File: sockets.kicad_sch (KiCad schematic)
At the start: 8 parts

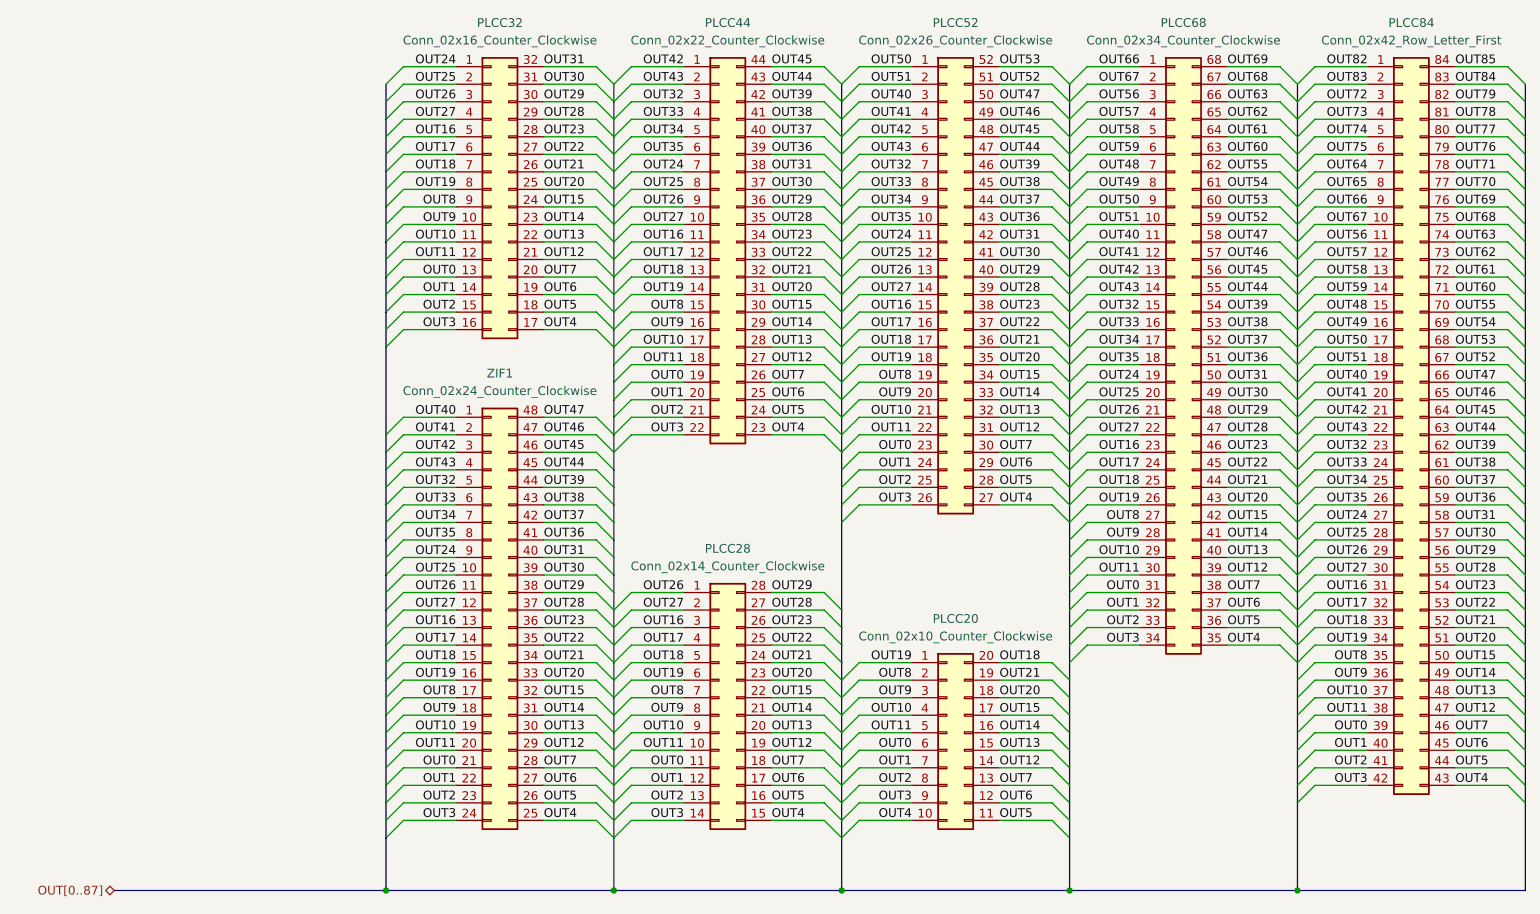
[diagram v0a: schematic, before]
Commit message: updates:
- update symbols and footprints from library
- re-correct 84 pin PLCC pin numbers
- reset transistors to TO-2whatever from SMD
- adjust position of DIN connectors, LEDs and their resistors (and 48 pin DIP and transistors and decoupling capacitors):  measured again.
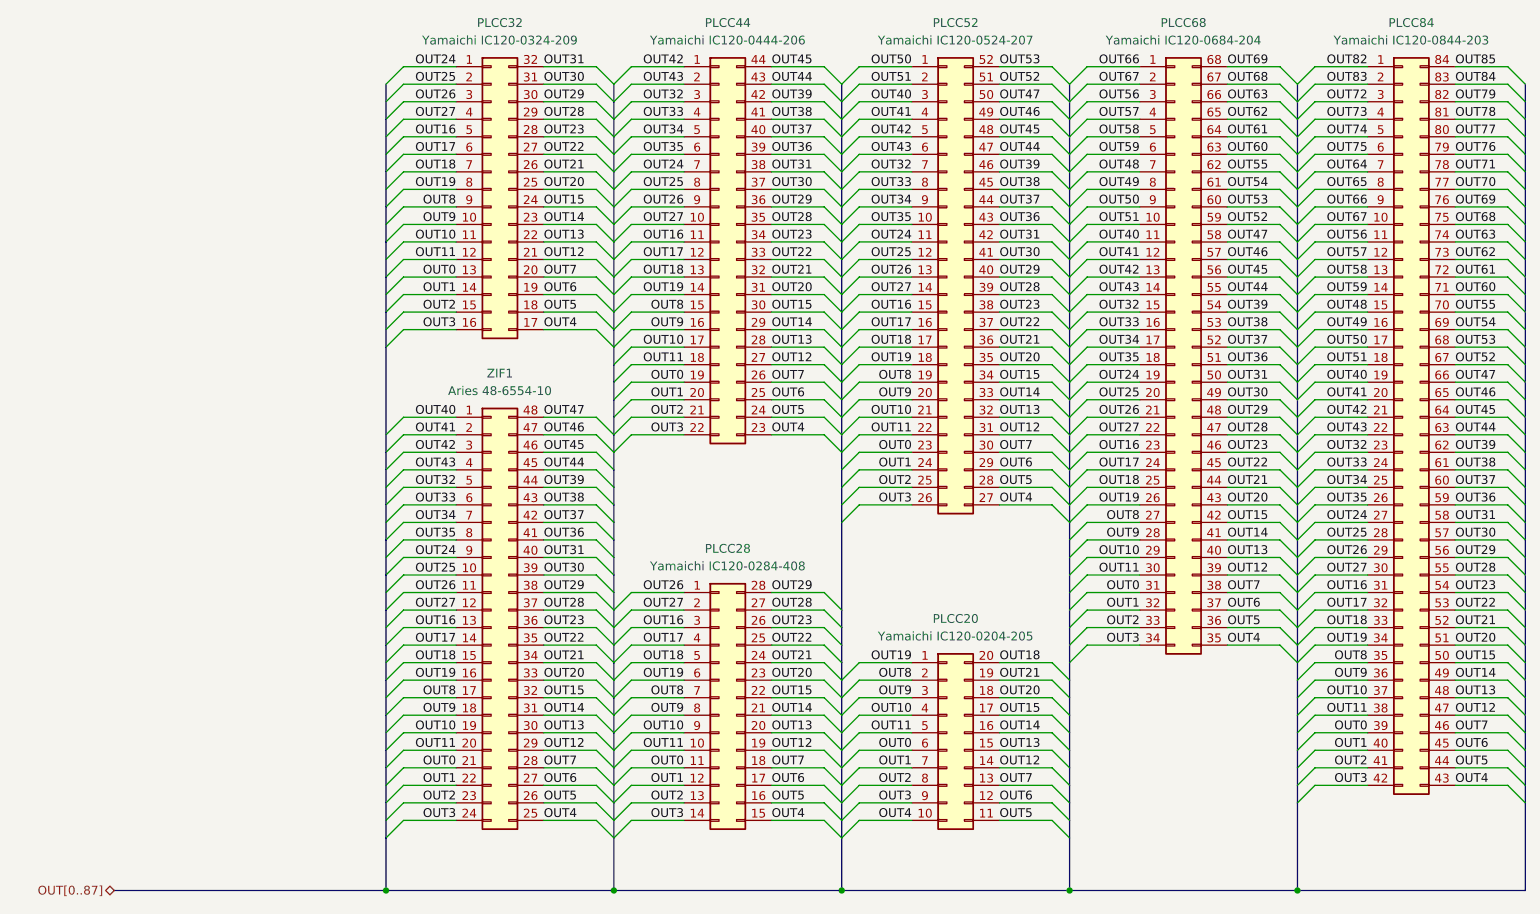
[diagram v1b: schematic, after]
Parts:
- PLCC20: value Conn_02x10_Counter_Clockwise -> Yamaichi IC120-0204-205
- PLCC28: value Conn_02x14_Counter_Clockwise -> Yamaichi IC120-0284-408
- PLCC32: value Conn_02x16_Counter_Clockwise -> Yamaichi IC120-0324-209
- PLCC44: value Conn_02x22_Counter_Clockwise -> Yamaichi IC120-0444-206
- PLCC52: value Conn_02x26_Counter_Clockwise -> Yamaichi IC120-0524-207
- PLCC68: value Conn_02x34_Counter_Clockwise -> Yamaichi IC120-0684-204
- PLCC84: value Conn_02x42_Row_Letter_First -> Yamaichi IC120-0844-203
- ZIF1: value Conn_02x24_Counter_Clockwise -> Aries 48-6554-10
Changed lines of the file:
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@@
 			)
 		)
-		(property "Value" "Conn_02x42_Row_Letter_First"
+		(property "Value" "Yamaichi IC120-0844-203"
 			(at 219.71 34.29 0)
 			(effects
@@
 			)
 		)
+		(pin "8"
+		)
+		(pin "26"
+		)
+		(pin "6"
+		)
+		(pin "30"
+		)
+		(pin "34"
+		)
+		(pin "14"
+		)
+		(pin "29"
+		)
+		(pin "15"
+		)
+		(pin "27"
+		)
+		(pin "12"
+		)
+		(pin "28"
+		)
+		(pin "23"
+		)
+		(pin "11"
+		)
+		(pin "10"
+		)
+		(pin "31"
+		)
+		(pin "32"
+		)
+		(pin "24"
+		)
+		(pin "7"
+		)
+		(pin "33"
+		)
+		(pin "25"
+		)
+		(pin "9"
+		)
+		(pin "13"
+		)
+		(pin "38"
+		)
+		(pin "39"
+		)
+		(pin "78"
+		)
+		(pin "77"
+		)
+		(pin "76"
+		)
+		(pin "81"
+		)
+		(pin "80"
+		)
+		(pin "79"
+		)
+		(pin "75"
+		)
+		(pin "1"
+		)
+		(pin "2"
+		)
+		(pin "84"
+		)
+		(pin "83"
+		)
+		(pin "82"
+		)
+		(pin "74"
+		)
+		(pin "73"
+		)
+		(pin "72"
+		)
+		(pin "71"
+		)
+		(pin "70"
+		)
+		(pin "69"
+		)
+		(pin "65"
+		)
+		(pin "64"
+		)
+		(pin "63"
+		)
+		(pin "35"
+		)
+		(pin "36"
+		)
+		(pin "16"
+		)
+		(pin "62"
+		)
+		(pin "61"
+		)
+		(pin "60"
+		)
+		(pin "68"
+		)
+		(pin "67"
+		)
+		(pin "66"
+		)
+		(pin "54"
+		)
+		(pin "53"
+		)
+		(pin "52"
+		)
+		(pin "47"
+		)
+		(pin "46"
+		)
+		(pin "45"
+		)
+		(pin "57"
+		)
+		(pin "56"
+		)
+		(pin "55"
+		)
+		(pin "17"
+		)
+		(pin "18"
+		)
+		(pin "19"
+		)
+		(pin "44"
+		)
+		(pin "43"
+		)
 		(pin "37"
 		)
-		(pin "8"
-		)
-		(pin "12"
-		)
-		(pin "80"
-		)
-		(pin "14"
-		)
-		(pin "31"
-		)
-		(pin "78"
-		)
-		(pin "84"
-		)
-		(pin "15"
+		(pin "20"
+		)
+		(pin "21"
+		)
+		(pin "22"
+		)
+		(pin "51"
+		)
+		(pin "50"
 		)
 		(pin "49"
 		)
-		(pin "28"
-		)
-		(pin "17"
-		)
-		(pin "44"
-		)
-		(pin "54"
-		)
-		(pin "9"
-		)
-		(pin "19"
-		)
-		(pin "32"
-		)
-		(pin "25"
+		(pin "40"
+		)
+		(pin "41"
+		)
+		(pin "42"
+		)
+		(pin "3"
+		)
+		(pin "4"
+		)
+		(pin "5"
+		)
+		(pin "59"
+		)
+		(pin "58"
 		)
 		(pin "48"
-		)
-		(pin "47"
-		)
-		(pin "45"
-		)
-		(pin "27"
-		)
-		(pin "24"
-		)
-		(pin "72"
-		)
-		(pin "10"
-		)
-		(pin "55"
-		)
-		(pin "57"
-		)
-		(pin "56"
-		)
-		(pin "20"
-		)
-		(pin "21"
-		)
-		(pin "46"
-		)
-		(pin "26"
-		)
-		(pin "39"
-		)
-		(pin "40"
-		)
-		(pin "67"
-		)
-		(pin "66"
-		)
-		(pin "59"
-		)
-		(pin "36"
-		)
-		(pin "41"
-		)
-		(pin "42"
-		)
-		(pin "75"
-		)
-		(pin "74"
-		)
-		(pin "65"
-		)
-		(pin "64"
-		)
-		(pin "73"
-		)
-		(pin "18"
-		)
-		(pin "58"
-		)
-		(pin "38"
-		)
-		(pin "81"
-		)
-		(pin "35"
-		)
-		(pin "29"
-		)
-		(pin "30"
-		)
-		(pin "61"
-		)
-		(pin "60"
-		)
-		(pin "1"
-		)
-		(pin "4"
-		)
-		(pin "3"
-		)
-		(pin "2"
-		)
-		(pin "83"
-		)
-		(pin "82"
-		)
-		(pin "13"
-		)
-		(pin "52"
-		)
-		(pin "51"
-		)
-		(pin "50"
-		)
-		(pin "33"
-		)
-		(pin "34"
-		)
-		(pin "22"
-		)
-		(pin "23"
-		)
-		(pin "7"
-		)
-		(pin "43"
-		)
-		(pin "69"
-		)
-		(pin "68"
-		)
-		(pin "53"
-		)
-		(pin "11"
-		)
-		(pin "71"
-		)
-		(pin "70"
-		)
-		(pin "63"
-		)
-		(pin "62"
-		)
-		(pin "16"
-		)
-		(pin "79"
-		)
-		(pin "77"
-		)
-		(pin "76"
-		)
-		(pin "5"
-		)
-		(pin "6"
 		)
 		(instances
@@
 			)
 		)
-		(property "Value" "Conn_02x24_Counter_Clockwise"
+		(property "Value" "Aries 48-6554-10"
 			(at 87.63 85.09 0)
 			(effects
@@
 			)
 		)
-		(property "Value" "Conn_02x34_Counter_Clockwise"
+		(property "Value" "Yamaichi IC120-0684-204"
 			(at 186.69 34.29 0)
 			(effects
@@
 		(on_board yes)
 		(dnp no)
-		(fields_autoplaced yes)
 		(property "Reference" "PLCC32"
 			(at 87.63 31.75 0)
@@
 			)
 		)
-		(property "Value" "Conn_02x16_Counter_Clockwise"
+		(property "Value" "Yamaichi IC120-0324-209"
 			(at 87.63 34.29 0)
 			(effects
@@
 			)
 		)
-		(property "Value" "Conn_02x14_Counter_Clockwise"
+		(property "Value" "Yamaichi IC120-0284-408"
 			(at 120.65 110.49 0)
 			(effects
@@
 			)
 		)
-		(property "Value" "Conn_02x26_Counter_Clockwise"
+		(property "Value" "Yamaichi IC120-0524-207"
 			(at 153.67 34.29 0)
 			(effects
@@
 			)
 		)
-		(property "Value" "Conn_02x10_Counter_Clockwise"
+		(property "Value" "Yamaichi IC120-0204-205"
 			(at 153.67 120.65 0)
 			(effects
@@
 			)
 		)
-		(property "Value" "Conn_02x22_Counter_Clockwise"
+		(property "Value" "Yamaichi IC120-0444-206"
 			(at 120.65 34.29 0)
 			(effects
